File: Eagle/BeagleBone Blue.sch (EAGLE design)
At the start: 122 parts, among them M1 JST_ZH_2, M2 JST_ZH_2, M3 JST_ZH_2, M4 JST_ZH_2, Q3 MOSFET-N, Q4 MOSFET-P

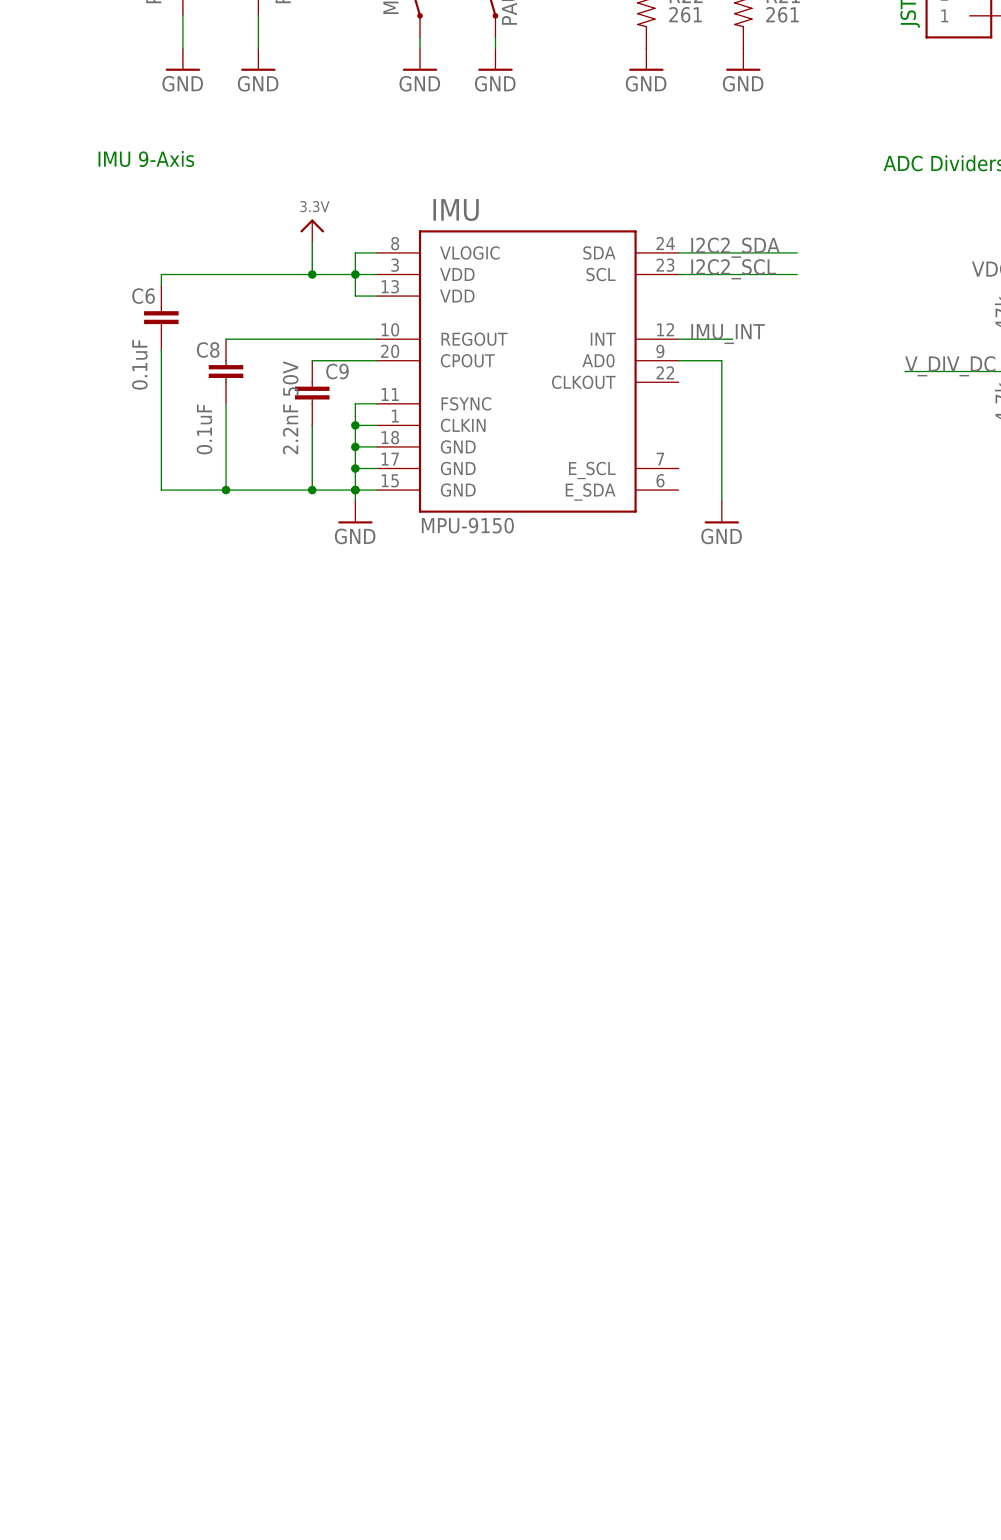
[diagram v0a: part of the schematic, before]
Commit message: added MPU-9250 component
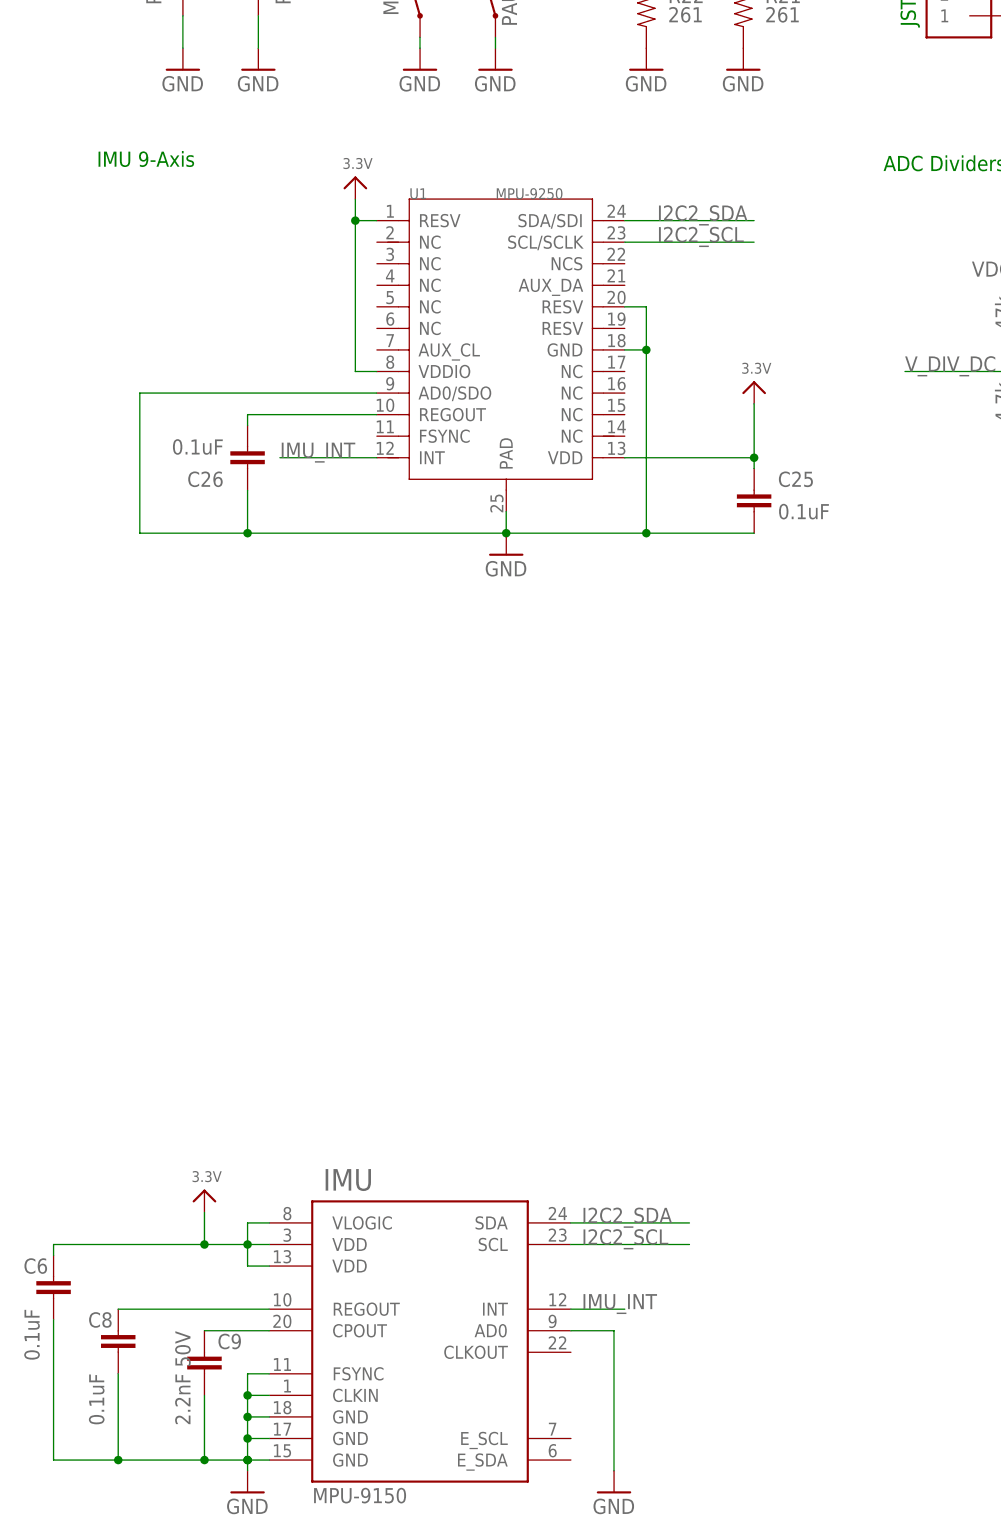
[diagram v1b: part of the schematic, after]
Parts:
- added C25, C26: 0.1uF, Strawson_Eagle_Lib:CAP0402-CAP
- added U1: MPU-9250, Strawson_Eagle_Lib:MPU-9250
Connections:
- new net N$70: C26.2, U1.REGOUT
- net 3.3V: now also C25.1, U1.RESV, U1.VDD, U1.VDDIO
- net GND: now also C25.2, C26.1, U1.AD0/SDO, U1.GND, U1.PAD, U1.RESV@2
- net I2C2_SCL: now also U1.SCL/SCLK
- net I2C2_SDA: now also U1.SDA/SDI
- net IMU_INT: now also U1.INT
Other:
- moved on the sheet: C6, C8, C9, IMU

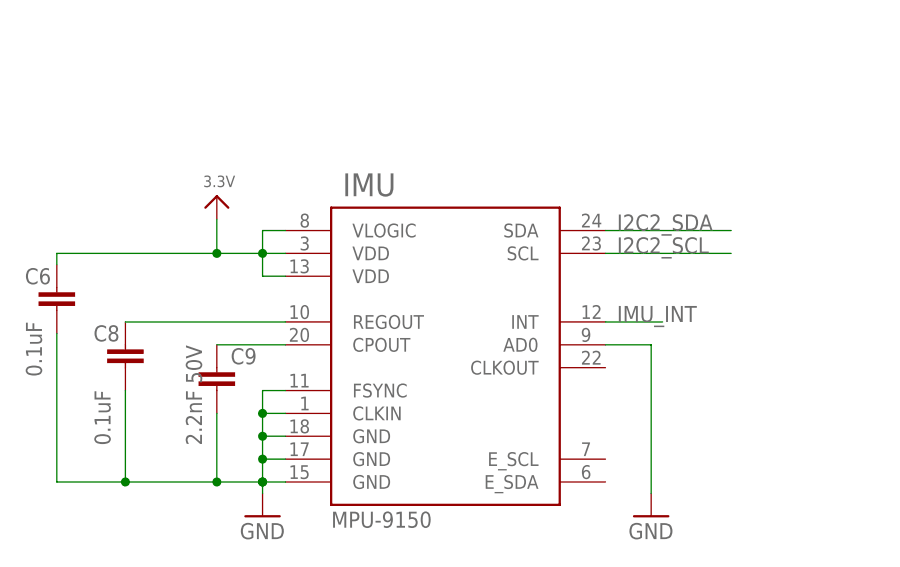
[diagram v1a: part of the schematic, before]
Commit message: update to MPU-9250
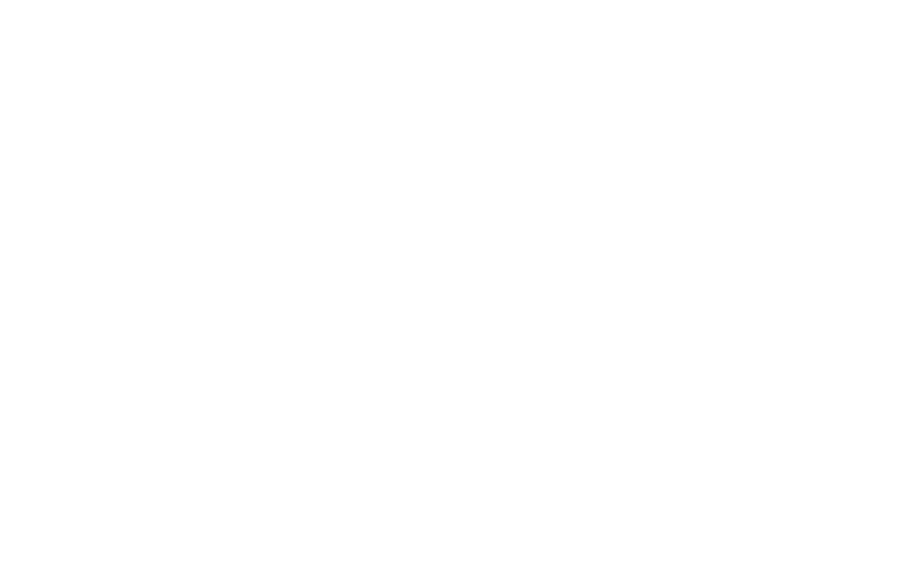
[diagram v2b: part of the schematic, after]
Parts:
- removed C6, C8: 0.1uF, Strawson_Eagle_Lib:CAP0402-CAP
- removed C9: 2.2nF 50V, Strawson_Eagle_Lib:CAP0402-CAP
- removed IMU: MPU-9150, SparkFun-Sensors:MPU-9150QFN-24-NP
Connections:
- removed net N$14: C8.1, IMU.REGOUT
- removed net N$15: C9.1, IMU.CPOUT
- net 3.3V: no longer C6.1, IMU.VDD@13, IMU.VDD@3, IMU.VLOGIC
- net GND: no longer C6.2, C8.2, C9.2, IMU.AD0, IMU.CLKIN, IMU.FSYNC, IMU.GND@15, IMU.GND@17, IMU.GND@18
- net I2C2_SCL: no longer IMU.SCL
- net I2C2_SDA: no longer IMU.SDA
- net IMU_INT: no longer IMU.INT
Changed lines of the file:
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@@
 <setting verticaltext="up"/>
 </settings>
-<grid distance="0.05" unitdist="inch" unit="inch" style="lines" multiple="1" display="no" altdistance="0.01" altunitdist="inch" altunit="inch"/>
+<grid distance="0.1" unitdist="inch" unit="inch" style="lines" multiple="1" display="no" altdistance="0.01" altunitdist="inch" altunit="inch"/>
 <layers>
 <layer number="1" name="Top" color="4" fill="1" visible="no" active="no"/>
@@
 <part name="U$3" library="microbuilder" deviceset="5.0V" device=""/>
 <part name="VDD_5V" library="microbuilder" deviceset="5.0V" device=""/>
-<part name="IMU" library="SparkFun-Sensors" deviceset="MPU-9150" device="QFN-24-NP" value="MPU-9150"/>
 <part name="H1" library="SparkFun" deviceset="TB6621FNG" device=""/>
 <part name="C2" library="Strawson_Eagle_Lib" deviceset="CAP" device="0402-CAP" value="0.1uF"/>
 <part name="H2" library="SparkFun" deviceset="TB6621FNG" device=""/>
 <part name="U$9" library="microbuilder" deviceset="3.3V" device=""/>
-<part name="GND16" library="SparkFun-Aesthetics" deviceset="GND" device=""/>
 <part name="GND18" library="SparkFun" deviceset="GND" device=""/>
 <part name="SUPPLY2" library="SparkFun-Aesthetics" deviceset="V_BATT" device=""/>
@@
 <part name="GND12" library="SparkFun" deviceset="GND" device=""/>
 <part name="GND14" library="SparkFun" deviceset="GND" device=""/>
-<part name="GND22" library="SparkFun-Aesthetics" deviceset="GND" device=""/>
 <part name="GND23" library="SparkFun-Aesthetics" deviceset="GND" device=""/>
-<part name="C6" library="Strawson_Eagle_Lib" deviceset="CAP" device="0402-CAP" value="0.1uF"/>
-<part name="3.3V" library="microbuilder" deviceset="3.3V" device=""/>
-<part name="C8" library="Strawson_Eagle_Lib" deviceset="CAP" device="0402-CAP" value="0.1uF"/>
-<part name="C9" library="Strawson_Eagle_Lib" deviceset="CAP" device="0402-CAP" value="2.2nF 50V"/>
 <part name="GND10" library="SparkFun-Aesthetics" deviceset="GND" device=""/>
 <part name="GND11" library="SparkFun-Aesthetics" deviceset="GND" device=""/>
@@
 <instance part="U$3" gate="G$1" x="8.89" y="173.99"/>
 <instance part="VDD_5V" gate="G$1" x="90.17" y="173.99"/>
-<instance part="IMU" gate="G$1" x="44.45" y="-85.09" smashed="yes">
-<attribute name="NAME" x="33.02" y="-66.04" size="2.54" layer="95"/>
-<attribute name="VALUE" x="31.75" y="-102.87" size="1.778" layer="96"/>
-</instance>
 <instance part="H1" gate="G$1" x="143.51" y="186.69" rot="R180"/>
 <instance part="C2" gate="G$1" x="107.95" y="166.37" smashed="yes" rot="MR180">
@@
 <instance part="H2" gate="G$1" x="143.51" y="224.79" rot="R180"/>
 <instance part="U$9" gate="G$1" x="107.95" y="241.3"/>
-<instance part="GND16" gate="1" x="24.13" y="-101.6"/>
 <instance part="GND18" gate="1" x="107.95" y="156.21"/>
 <instance part="SUPPLY2" gate="G$1" x="124.46" y="241.3"/>
@@
 <instance part="GND12" gate="1" x="102.87" y="156.21"/>
 <instance part="GND14" gate="1" x="162.56" y="156.21"/>
-<instance part="GND22" gate="1" x="67.31" y="-101.6"/>
 <instance part="GND23" gate="1" x="80.01" y="247.65" rot="R180"/>
-<instance part="C6" gate="G$1" x="1.27" y="-78.74" smashed="yes">
-<attribute name="NAME" x="-2.286" y="-75.819" size="1.778" layer="95"/>
-<attribute name="VALUE" x="-0.381" y="-86.106" size="1.778" layer="96" rot="R90"/>
-</instance>
-<instance part="3.3V" gate="G$1" x="19.05" y="-68.58"/>
-<instance part="C8" gate="G$1" x="8.89" y="-85.09" smashed="yes">
-<attribute name="NAME" x="5.334" y="-82.169" size="1.778" layer="95"/>
-<attribute name="VALUE" x="7.239" y="-93.726" size="1.778" layer="96" rot="R90"/>
-</instance>
-<instance part="C9" gate="G$1" x="19.05" y="-87.63" smashed="yes">
-<attribute name="NAME" x="20.574" y="-84.709" size="1.778" layer="95"/>
-<attribute name="VALUE" x="17.399" y="-93.726" size="1.778" layer="96" rot="R90"/>
-</instance>
 <instance part="GND10" gate="1" x="80.01" y="176.53" rot="R180"/>
 <instance part="GND11" gate="1" x="19.05" y="176.53" rot="R180"/>
@@
 <wire x1="85.09" y1="171.45" x2="85.09" y2="173.99" width="0.1524" layer="91"/>
 <pinref part="U$11" gate="G$1" pin="3.3V"/>
-</segment>
-<segment>
-<pinref part="IMU" gate="G$1" pin="VDD@13"/>
-<pinref part="IMU" gate="G$1" pin="VLOGIC"/>
-<pinref part="IMU" gate="G$1" pin="VDD@3"/>
-<pinref part="C6" gate="G$1" pin="1"/>
-<wire x1="26.67" y1="-72.39" x2="24.13" y2="-72.39" width="0.1524" layer="91"/>
-<pinref part="3.3V" gate="G$1" pin="3.3V"/>
-<wire x1="19.05" y1="-72.39" x2="19.05" y2="-68.58" width="0.1524" layer="91"/>
-<wire x1="26.67" y1="-69.85" x2="24.13" y2="-69.85" width="0.1524" layer="91"/>
-<wire x1="24.13" y1="-69.85" x2="24.13" y2="-72.39" width="0.1524" layer="91"/>
-<wire x1="24.13" y1="-72.39" x2="24.13" y2="-74.93" width="0.1524" layer="91"/>
-<wire x1="24.13" y1="-74.93" x2="26.67" y2="-74.93" width="0.1524" layer="91"/>
-<junction x="24.13" y="-72.39"/>
-<wire x1="24.13" y1="-72.39" x2="19.05" y2="-72.39" width="0.1524" layer="91"/>
-<junction x="19.05" y="-72.39"/>
-<wire x1="19.05" y1="-72.39" x2="1.27" y2="-72.39" width="0.1524" layer="91"/>
-<wire x1="1.27" y1="-72.39" x2="1.27" y2="-73.66" width="0.1524" layer="91"/>
 </segment>
 <segment>
@@
 </segment>
 </net>
-<net name="N$14" class="0">
-<segment>
-<pinref part="C8" gate="G$1" pin="1"/>
-<pinref part="IMU" gate="G$1" pin="REGOUT"/>
-<wire x1="8.89" y1="-80.01" x2="26.67" y2="-80.01" width="0.1524" layer="91"/>
-</segment>
-</net>
-<net name="N$15" class="0">
-<segment>
-<pinref part="IMU" gate="G$1" pin="CPOUT"/>
-<pinref part="C9" gate="G$1" pin="1"/>
-<wire x1="26.67" y1="-82.55" x2="19.05" y2="-82.55" width="0.1524" layer="91"/>
-</segment>
-</net>
 <net name="I2C2_SCL" class="0">
-<segment>
-<pinref part="IMU" gate="G$1" pin="SCL"/>
-<wire x1="62.23" y1="-72.39" x2="76.2" y2="-72.39" width="0.1524" layer="91"/>
-<label x="63.5" y="-72.39" size="1.778" layer="95"/>
-</segment>
 <segment>
 <pinref part="R11" gate="G$1" pin="1"/>
@@
 </net>
 <net name="I2C2_SDA" class="0">
-<segment>
-<pinref part="IMU" gate="G$1" pin="SDA"/>
-<wire x1="62.23" y1="-69.85" x2="76.2" y2="-69.85" width="0.1524" layer="91"/>
-<label x="63.5" y="-69.85" size="1.778" layer="95"/>
-</segment>
 <segment>
 <pinref part="R10" gate="G$1" pin="2"/>
@@
 </segment>
 <segment>
-<pinref part="IMU" gate="G$1" pin="AD0"/>
-<pinref part="GND22" gate="1" pin="GND"/>
-<wire x1="62.23" y1="-82.55" x2="67.31" y2="-82.55" width="0.1524" layer="91"/>
-<wire x1="67.31" y1="-82.55" x2="67.31" y2="-99.06" width="0.1524" layer="91"/>
-</segment>
-<segment>
 <wire x1="66.04" y1="240.03" x2="80.01" y2="240.03" width="0.1524" layer="91"/>
 <wire x1="80.01" y1="240.03" x2="80.01" y2="245.11" width="0.1524" layer="91"/>
 <pinref part="GND23" gate="1" pin="GND"/>
-</segment>
-<segment>
-<pinref part="IMU" gate="G$1" pin="GND@15"/>
-<pinref part="IMU" gate="G$1" pin="GND@17"/>
-<pinref part="IMU" gate="G$1" pin="GND@18"/>
-<pinref part="GND16" gate="1" pin="GND"/>
-<pinref part="IMU" gate="G$1" pin="CLKIN"/>
-<pinref part="C8" gate="G$1" pin="2"/>
-<wire x1="8.89" y1="-87.63" x2="8.89" y2="-97.79" width="0.1524" layer="91"/>
-<wire x1="8.89" y1="-97.79" x2="19.05" y2="-97.79" width="0.1524" layer="91"/>
-<pinref part="C6" gate="G$1" pin="2"/>
-<wire x1="19.05" y1="-97.79" x2="24.13" y2="-97.79" width="0.1524" layer="91"/>
-<wire x1="24.13" y1="-97.79" x2="24.13" y2="-99.06" width="0.1524" layer="91"/>
-<wire x1="1.27" y1="-81.28" x2="1.27" y2="-97.79" width="0.1524" layer="91"/>
-<wire x1="1.27" y1="-97.79" x2="8.89" y2="-97.79" width="0.1524" layer="91"/>
-<pinref part="C9" gate="G$1" pin="2"/>
-<wire x1="19.05" y1="-90.17" x2="19.05" y2="-97.79" width="0.1524" layer="91"/>
-<pinref part="IMU" gate="G$1" pin="FSYNC"/>
-<junction x="8.89" y="-97.79"/>
-<junction x="19.05" y="-97.79"/>
-<wire x1="26.67" y1="-87.63" x2="24.13" y2="-87.63" width="0.1524" layer="91"/>
-<wire x1="24.13" y1="-87.63" x2="24.13" y2="-90.17" width="0.1524" layer="91"/>
-<wire x1="24.13" y1="-90.17" x2="26.67" y2="-90.17" width="0.1524" layer="91"/>
-<wire x1="24.13" y1="-90.17" x2="24.13" y2="-92.71" width="0.1524" layer="91"/>
-<wire x1="24.13" y1="-92.71" x2="26.67" y2="-92.71" width="0.1524" layer="91"/>
-<wire x1="24.13" y1="-92.71" x2="24.13" y2="-95.25" width="0.1524" layer="91"/>
-<wire x1="24.13" y1="-95.25" x2="26.67" y2="-95.25" width="0.1524" layer="91"/>
-<wire x1="24.13" y1="-95.25" x2="24.13" y2="-97.79" width="0.1524" layer="91"/>
-<wire x1="24.13" y1="-97.79" x2="26.67" y2="-97.79" width="0.1524" layer="91"/>
-<junction x="24.13" y="-90.17"/>
-<junction x="24.13" y="-92.71"/>
-<junction x="24.13" y="-95.25"/>
-<junction x="24.13" y="-97.79"/>
-<junction x="24.13" y="-97.79"/>
 </segment>
 <segment>
@@
 </segment>
 <segment>
-<pinref part="IMU" gate="G$1" pin="INT"/>
-<wire x1="62.23" y1="-80.01" x2="68.58" y2="-80.01" width="0.1524" layer="91"/>
-<label x="63.5" y="-80.01" size="1.778" layer="95"/>
-</segment>
-<segment>
